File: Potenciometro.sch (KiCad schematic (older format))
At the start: 1 part

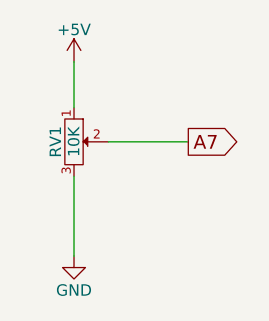
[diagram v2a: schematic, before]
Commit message: corregidos valores en esquema y simbolos corruptos
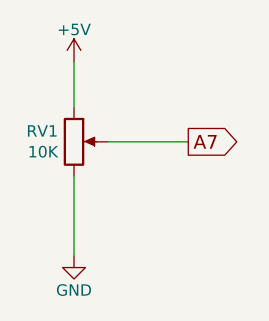
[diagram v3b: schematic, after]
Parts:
- removed RV1: 10K, Potenciometros:ALP_RK09K111, symbol POT-RESCUE-Nano_PB
- added RV1: 10K, Potenciometros:ALP_RK09K111, symbol POT
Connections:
- net +5V: now also RV1.1
- net A7: now also RV1.2
- net GND: now also RV1.3
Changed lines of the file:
@@
 EESchema Schematic File Version 2
-LIBS:Interfaces
 LIBS:Nano_PB-rescue
+LIBS:Interfaces
 LIBS:Sensores
 LIBS:power
@@
 LIBS:matriz_led
 LIBS:Pasivos
+LIBS:Reles
 LIBS:Nano_PB-cache
 EELAYER 26 0
@@
 $EndDescr
 $Comp
-L POT-RESCUE-Nano_PB RV1
-U 1 1 5793F630
-P 2550 2500
-F 0 "RV1" H 2550 2420 50  0000 C CNN
-F 1 "10K" H 2550 2500 50  0000 C CNN
-F 2 "Potenciometros:ALP_RK09K111" H 2550 2500 50  0001 C CNN
-F 3 "" H 2550 2500 50  0000 C CNN
-F 4 "ALPS" H 2550 2500 60  0001 C CNN "Fabricante"
-F 5 "RK09K1110A0J" H 2550 2500 60  0001 C CNN "Ref"
-F 6 "0,05W" H 2550 2500 60  0001 C CNN "Potencia"
-F 7 "20%" H 2550 2500 60  0001 C CNN "Tolerancia"
-F 8 "RS" H 2550 2500 60  0001 C CNN "Provedor"
-F 9 "729-3622" H 2550 2500 60  0001 C CNN "Ref_Proveedor"
-	1    2550 2500
-	0    1    1    0
-$EndComp
-$Comp
-L +5V #PWR050
+L +5V #PWR042
 U 1 1 5793F637
 P 2550 2150
-F 0 "#PWR050" H 2550 2000 50  0001 C CNN
+F 0 "#PWR042" H 2550 2000 50  0001 C CNN
 F 1 "+5V" H 2550 2290 50  0000 C CNN
 F 2 "" H 2550 2150 50  0000 C CNN
@@
 $EndComp
 $Comp
-L GND #PWR051
+L GND #PWR043
 U 1 1 5793F63D
 P 2550 3000
-F 0 "#PWR051" H 2550 2750 50  0001 C CNN
+F 0 "#PWR043" H 2550 2750 50  0001 C CNN
 F 1 "GND" H 2550 2850 50  0000 C CNN
 F 2 "" H 2550 3000 50  0000 C CNN
@@
 $Bitmap
 Pos 7500 4400
-Scale 0,350000
+Scale 0,000000
 Data
 89 50 4E 47 0D 0A 1A 0A 00 00 00 0D 49 48 44 52 00 00 01 D5 00 00 01 ED 08 06 00 00 00 4F 90 E4
@@
 EndData
 $EndBitmap
+$Comp
+L POT RV1
+U 1 1 58BA27E0
+P 2550 2500
+F 0 "RV1" H 2480 2546 50  0000 R CNN
+F 1 "10K" H 2480 2455 50  0000 R CNN
+F 2 "Potenciometros:ALP_RK09K111" H 250 200 50  0001 C CNN
+F 3 "" H 250 200 50  0001 C CNN
+F 4 "ALPS" H 2550 2500 60  0001 C CNN "Fabricante"
+F 5 "RK09K1110A0J" H 2550 2500 60  0001 C CNN "Ref"
+F 6 "0,05W" H 2550 2500 60  0001 C CNN "Potencia"
+F 7 "20%" H 2550 2500 60  0001 C CNN "Tolerancia"
+F 8 "RS" H 2550 2500 60  0001 C CNN "Provedor"
+F 9 "729-3622" H 2550 2500 60  0001 C CNN "Ref_Proveedor"
+	1    2550 2500
+	1    0    0    -1
+$EndComp
 $EndSCHEMATC
